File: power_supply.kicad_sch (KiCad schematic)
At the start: 54 parts, among them Q1 SQS401EN-T1_BE3, U1 STUSB4500_QFN, U2 SIC477ED-T1-GE3

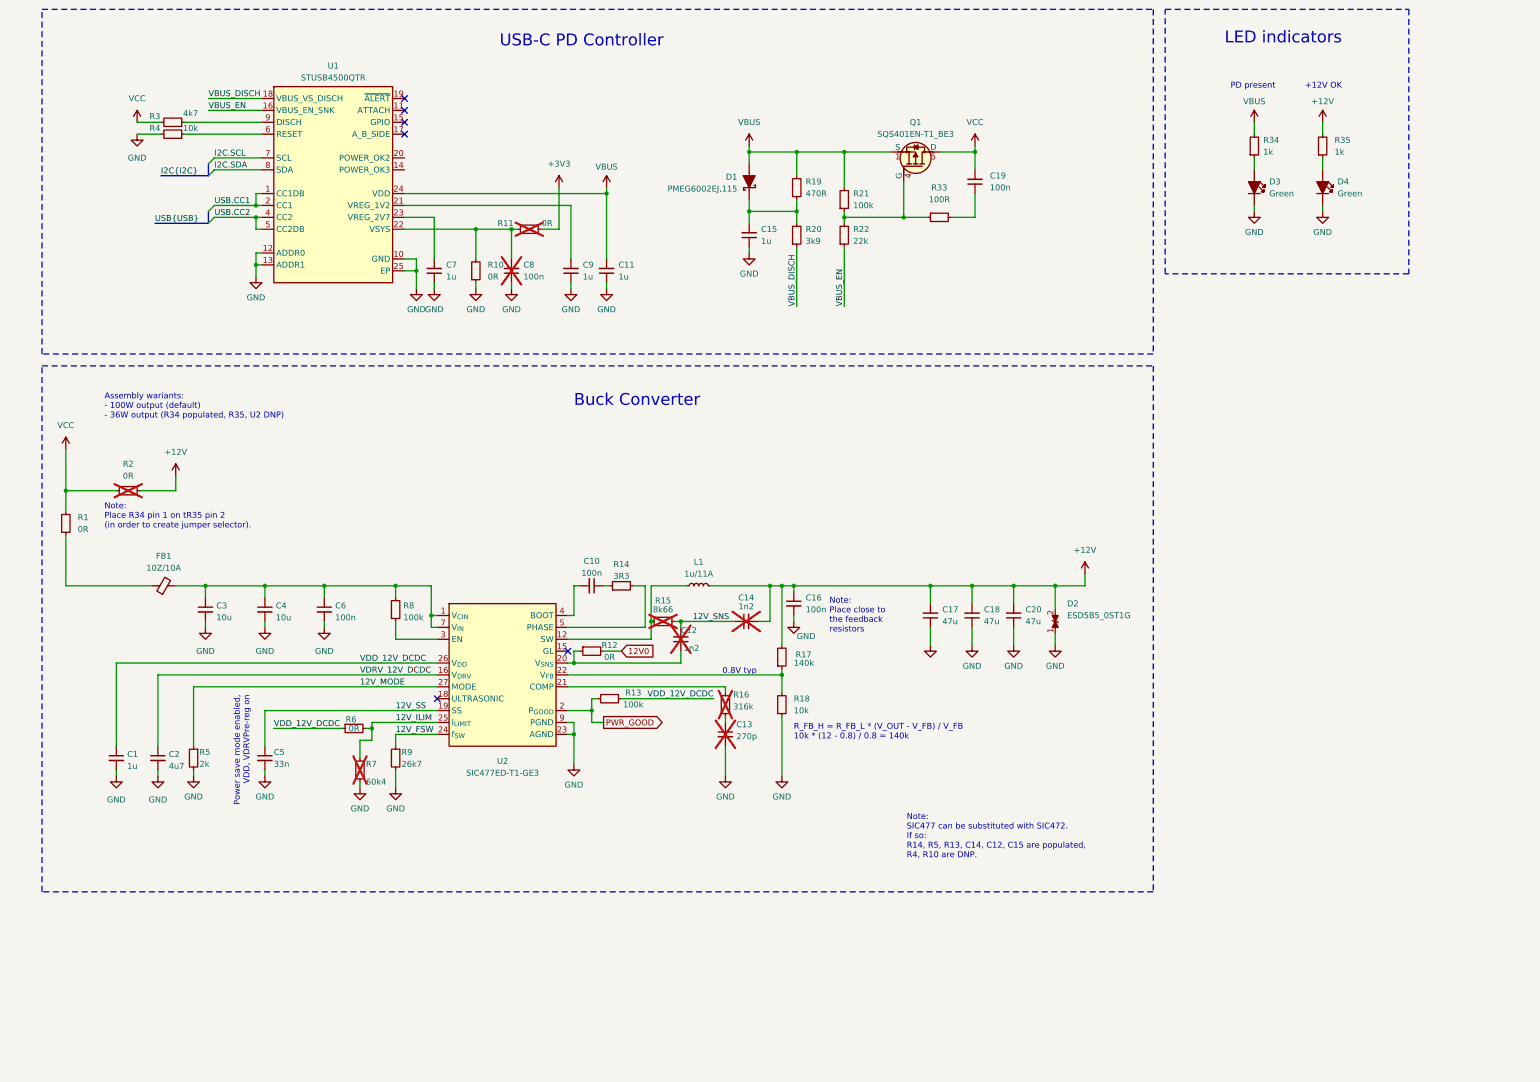
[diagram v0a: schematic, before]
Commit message: [#57006] Reorganize structure
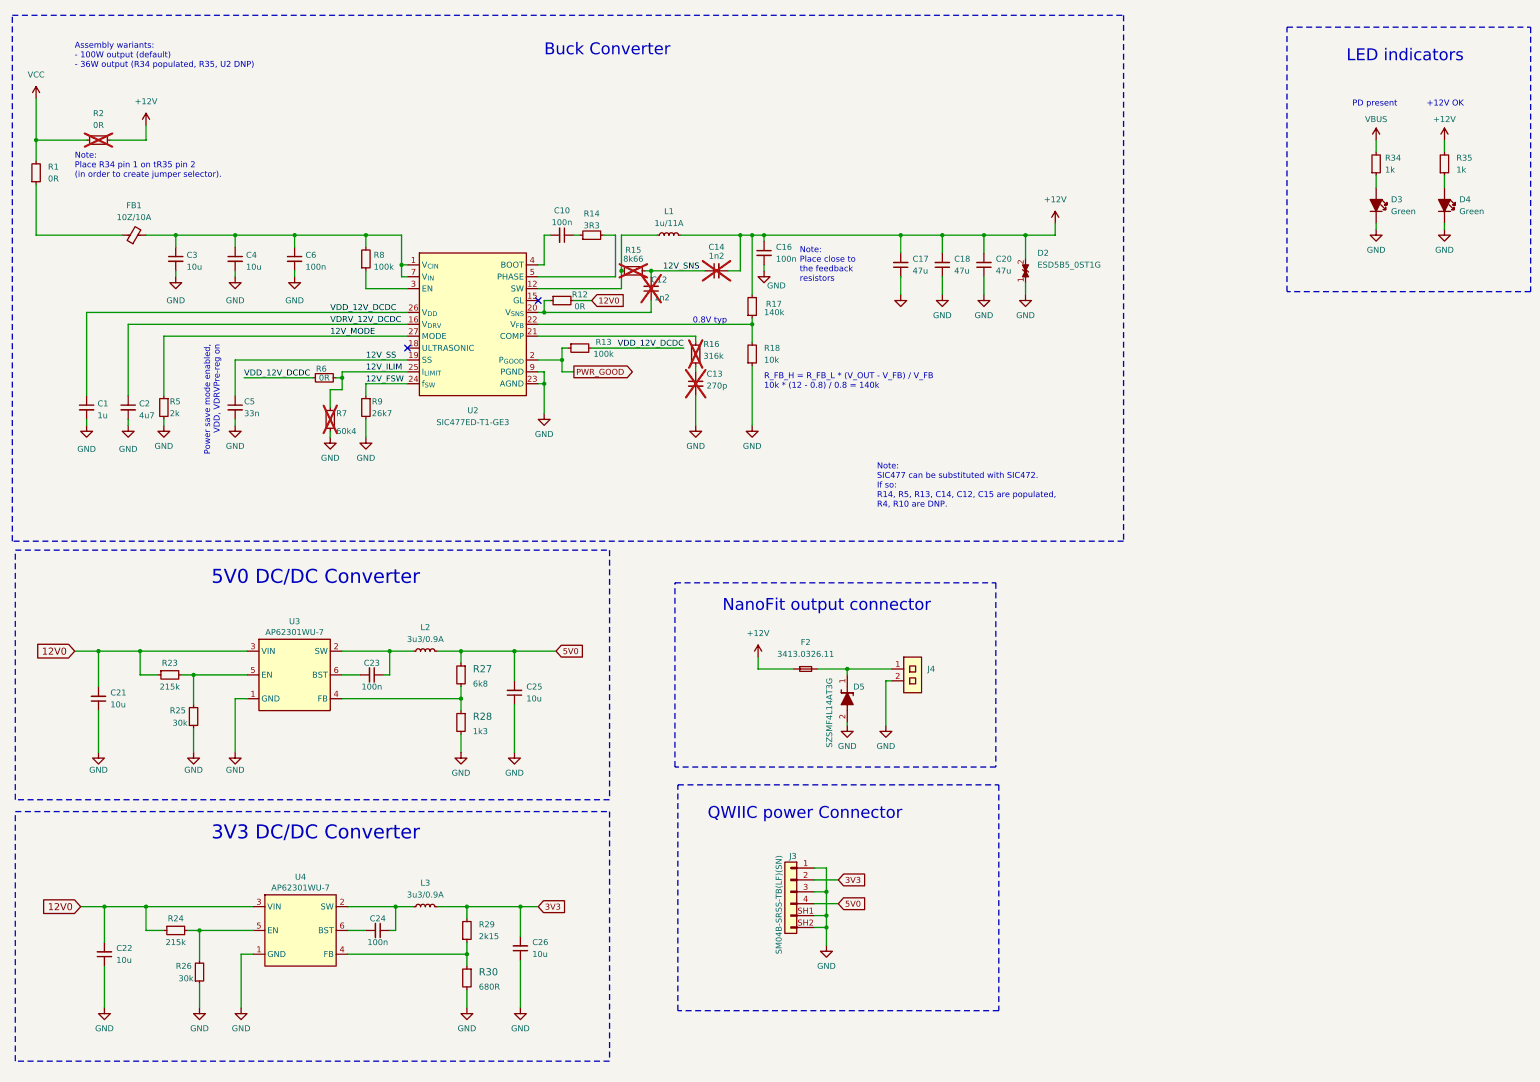
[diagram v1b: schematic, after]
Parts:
- removed C11, C15, C7, C9: C_1u_0402, antmicro-footprints:C_0402_1005Metric, symbol antmicroCapacitors0402:C_1u_0402
- removed C19: C_100n_50V_X8L_0402, antmicro-footprints:C_0402_1005Metric, symbol antmicroCapacitors0402:C_100n_50V_X8L_0402
- removed C8: C_100n_0402, antmicro-footprints:C_0402_1005Metric, symbol antmicroCapacitors0402:C_100n_0402
- removed D1: PMEG6002EJ,115, antmicro-footprints:D_SOD-323F, symbol antmicroDiodesRectifiersSingle:PMEG6002EJ,115
- removed Q1: SQS401EN-T1_BE3, antmicro-footprints:Vishay_PowerPAK_1212-8_Single, symbol antmicroTransistorsFETsMOSFETsSingle:SQS401EN-T1_BE3
- removed R10, R11: R_0R_0402, antmicro-footprints:R_0402_1005Metric, symbol antmicroResistors0402:R_0R_0402
- removed R19: R_470R_0603, antmicro-footprints:R_0603_1608Metric, symbol antmicroResistors0603:R_470R_0603
- removed R20: R_3k9_0603, antmicro-footprints:R_0603_1608Metric, symbol antmicroResistors0603:R_3k9_0603
- removed R21: R_100k_0402, antmicro-footprints:R_0402_1005Metric, symbol antmicroResistors0402:R_100k_0402
- removed R22: R_22k_0402, antmicro-footprints:R_0402_1005Metric, symbol antmicroResistors0402:R_22k_0402
- removed R3: R_4k7_0805, antmicro-footprints:R_0805_2012Metric, symbol antmicroResistorsmisc:R_4k7_0805
- removed R33: R_100R_0402, antmicro-footprints:R_0402_1005Metric, symbol antmicroResistors0402:R_100R_0402
- removed R4: R_10k_0402, antmicro-footprints:R_0402_1005Metric, symbol antmicroResistors0402:R_10k_0402
- removed U1: STUSB4500_QFN, antmicro-footprints:QFN-24-1EP_4x4mm_P0.5_EP2.1x2.1mm, symbol antmicroPMICPowerDistributionSwitchesLoadDrivers:STUSB4500_QFN
- added C21, C22, C25, C26: C_10u_25V_0603, antmicro-footprints:C_0603_1608Metric, symbol antmicroCapacitors0603:C_10u_25V_0603
- added C23, C24: C_100n_50V_X8L_0402, antmicro-footprints:C_0402_1005Metric, symbol antmicroCapacitors0402:C_100n_50V_X8L_0402
- added D5: SZSMF4L14AT3G, antmicro-footprints:SOD-123FL, symbol antmicroTVSDiodes:SZSMF4L14AT3G
- added F2: F_7A_1206, antmicro-footprints:F_1206_3216Metric, symbol antmicroFuses:F_7A_1206
- added J3: JST_SH_1x4_SM04B-SRSS-TB-LF-SN, antmicro-footprints:Conn_JST_SH_1x4_SM04B-SRSS-TB-LF-SN, symbol antmicroWire2BoardConnectors:JST_SH_1x4_SM04B-SRSS-TB-LF-SN
- added J4: Molex_Nano-Fit_1x2_105313-2202_Horizontal, antmicro-footprints:Conn_Molex_Nano-Fit_1x2_105313-2202_Horizontal, symbol antmicroWire2BoardConnectors:Molex_Nano-Fit_1x2_105313-2202_Horizontal
- added L2, L3: L_3u3_0.9A_0805, antmicro-footprints:L_0805_2012Metric, symbol antmicroFixedInductors:L_3u3_0.9A_0805
- added R23, R24: R_215k_0402, antmicro-footprints:R_0402_1005Metric, symbol antmicroResistors0402:R_215k_0402
- added R25, R26: R_30R_0402, antmicro-footprints:R_0402_1005Metric, symbol antmicroResistors0402:R_30k_0402
- added R27: R_6k8_0402, antmicro-footprints:R_0402_1005Metric, symbol antmicroResistors0402:R_6k8_0402
- added R28: R_1k3_0402, antmicro-footprints:R_0402_1005Metric, symbol antmicroResistors0402:R_1k3_0402
- added R29: R_template_name_0402, antmicro-footprints:R_0402_1005Metric, symbol antmicroResistors0402:R_2k15_0402
- added R30: R_680R_0402, antmicro-footprints:R_0402_1005Metric, symbol antmicroResistors0402:R_680R_0402
- added U3, U4: AP62301WU-7, antmicro-footprints:TSOT23-6, symbol antmicroDCDCConverters:AP62301_TSOT
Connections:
- net +12V: now also F2.1
- net 12V0: now also C21.2, C22.2, R23.1, R24.1, U3.3 (VIN), U4.3 (VIN)
- net GND: now also C21.1, C22.1, C25.1, C26.1, D5.2, J3.1, J3.3, J3.SH1, J3.SH2, J4.2, R25.1, R26.1, R28.2, R30.2, U3.1 (GND), U4.1 (GND)
- new net: R27.2, R28.1, U3.4 (FB)
- new net: C24.1, L3.1, U4.2 (SW)
- new net: C24.2, U4.6 (BST)
- new net: D5.1, F2.2, J4.1
- new net: R29.1, R30.1, U4.4 (FB)
- new net: R23.2, R25.2, U3.5 (EN)
- new net: R24.2, R26.2, U4.5 (EN)
- new net: C23.1, L2.1, U3.2 (SW)
- new net: C23.2, U3.6 (BST)
- new net 3V3: C26.2, J3.2, L3.2, R29.2
- new net 5V0: C25.2, J3.4, L2.2, R27.1
- no-connect marks 6 -> 2
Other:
- note added: "3V3 DC/DC Converter"
- note added: "5V0 DC/DC Converter"
- note added: "NanoFit output connector"
- note added: "QWIIC power Connector"
- note removed: "USB-C PD Controller"
- company: (none) -> Antmicro
- title: (none) -> USB-C-power-adapter
- moved on the sheet: C1, C10, C12, C13, C14, C16, C17, C18, C2, C20, C3, C4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

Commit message: [#57006] Clean ERC warnings
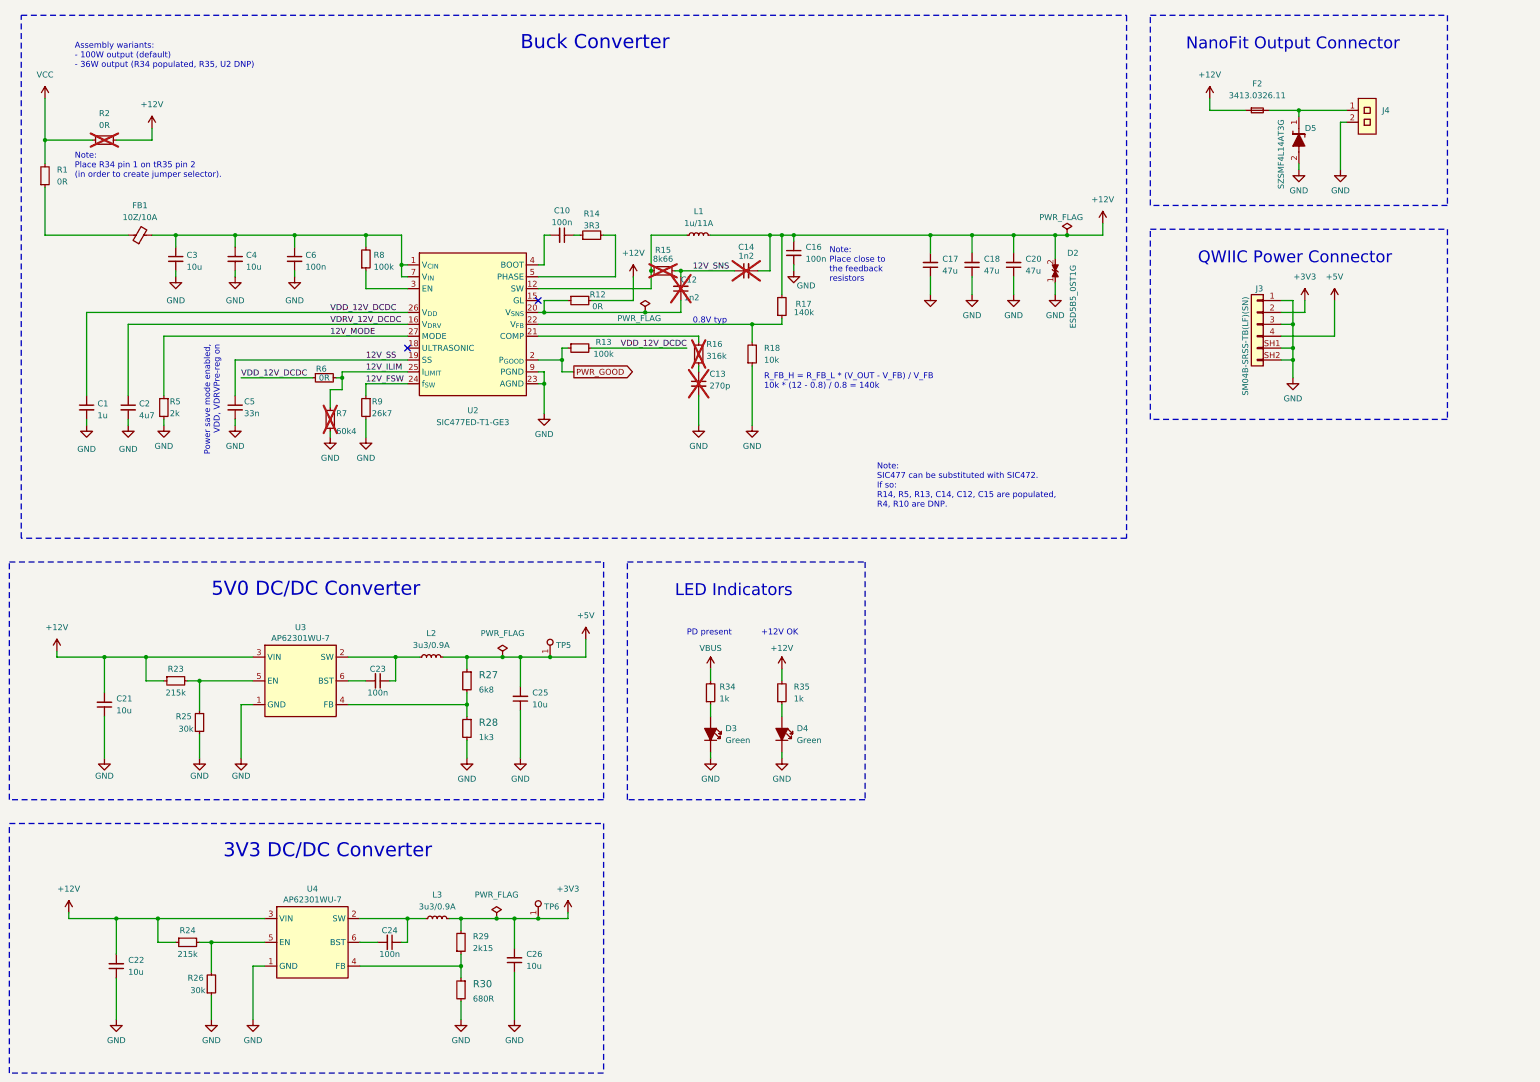
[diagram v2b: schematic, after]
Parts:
- added TP5, TP6: TP_0.75mm_SMD, antmicro-footprints:TP_SMD_0.75mm, symbol antmicroTestPoints:TP_0.75mm_SMD
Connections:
- net 12V0 is gone; now on net +12V: C21.2, C22.2, R12.2, R23.1, R24.1, U3.3 (VIN), U4.3 (VIN)
- net 3V3 renamed +3V3
- net +3V3: now also TP6.1
- net 5V0 renamed +5V
- net +5V: now also TP5.1
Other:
- note added: "LED Indicators"
- note added: "NanoFit Output Connector"
- note added: "QWIIC Power Connector"
- note removed: "LED indicators"
- note removed: "NanoFit output connector"
- note removed: "QWIIC power Connector"
- moved on the sheet: C12, C13, C14, C16, C17, C18, C20, C21, C22, C23, C24, C25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

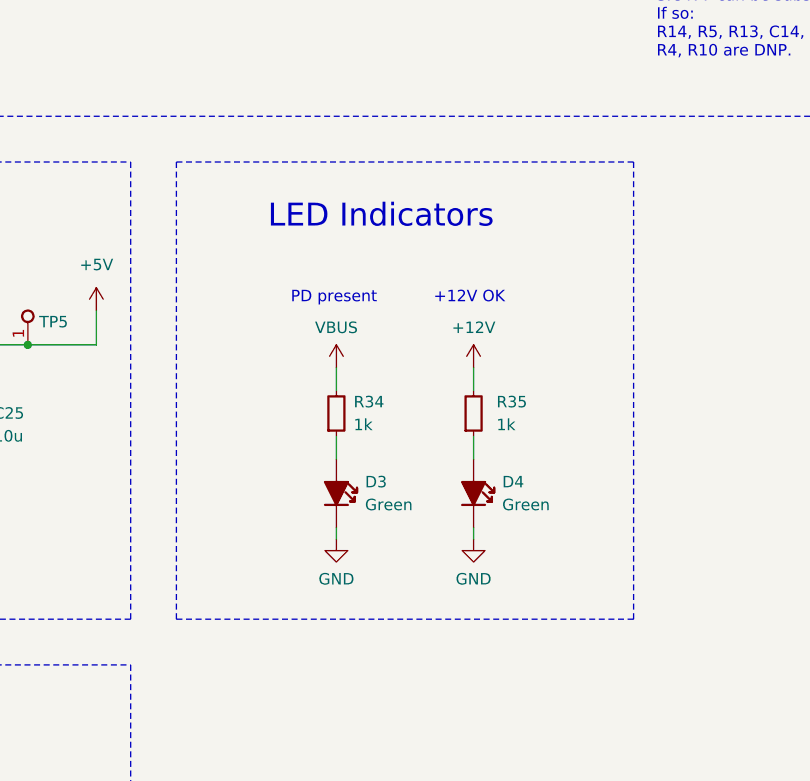
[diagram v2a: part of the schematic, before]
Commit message: [#57006] Add LEDs on POWER_GOOD signals
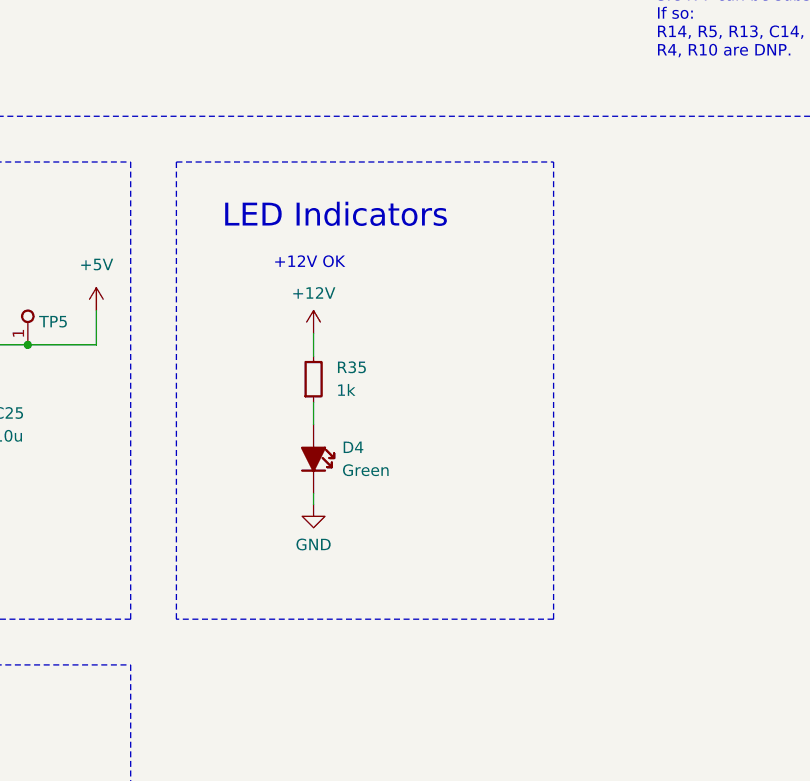
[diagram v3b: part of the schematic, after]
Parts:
- removed D3: LED_G_0603_LG_L29K-G2J1-24-Z, antmicro-footprints:LED_0603_1608Metric_G, symbol antmicroLEDIndicationDiscrete:LED_G_0603_LG_L29K-G2J1-24-Z
- removed R34: R_2k2_0402, antmicro-footprints:R_0402_1005Metric, symbol antmicroResistors0402:R_1k_0402
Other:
- note removed: "PD present"
- moved on the sheet: D4, R35
